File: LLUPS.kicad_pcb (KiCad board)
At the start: 2 copper layers, 90 x 58 mm, 39 parts, among them J1 USB_C, J2 Output, J3 Debug, Q1 FS8205A, U1 USBLC6-2SC6, U2 BQ24072, U3 HY2113-KB5B, U4 MT3608, U5 AP2112K-3.3, U6 LN61CN3302MR-G

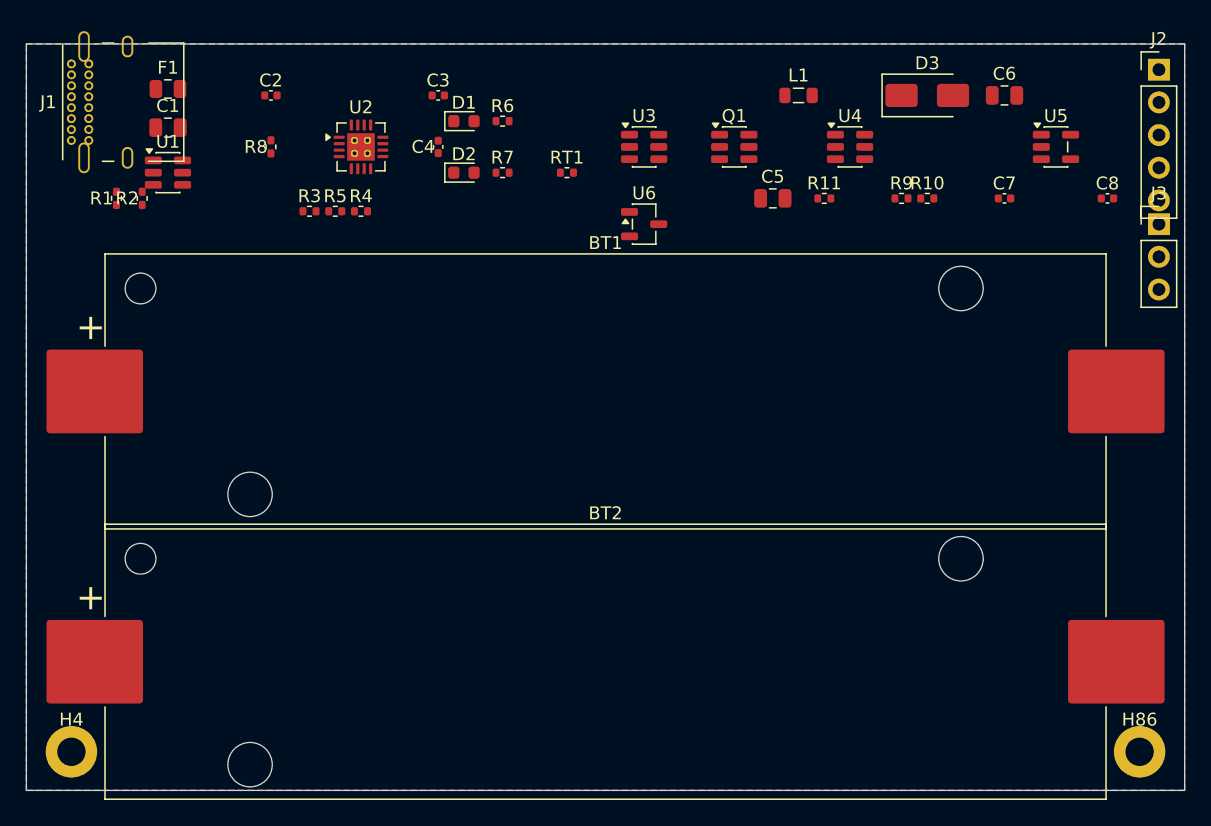
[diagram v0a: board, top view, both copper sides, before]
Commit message: Add PCB scoring framework and fix power trace widths
- scoring/ module with 6 checks: trace widths, DRC, connectivity,
  placement, vias, routing efficiency
- score_layout.py orchestrator with JSON output and --compare
- Fix power trace widths: 0.5mm → 1.0mm, 0.8mm → 1.2mm (spec: ≥1mm)
- Add 18 thermal vias under U2 (BQ24072) and U4 (MT3608)
- Score improved from 56.2 → 84.9/100

Co-Authored-By: Claude Opus 4.6 <noreply@anthropic.com>
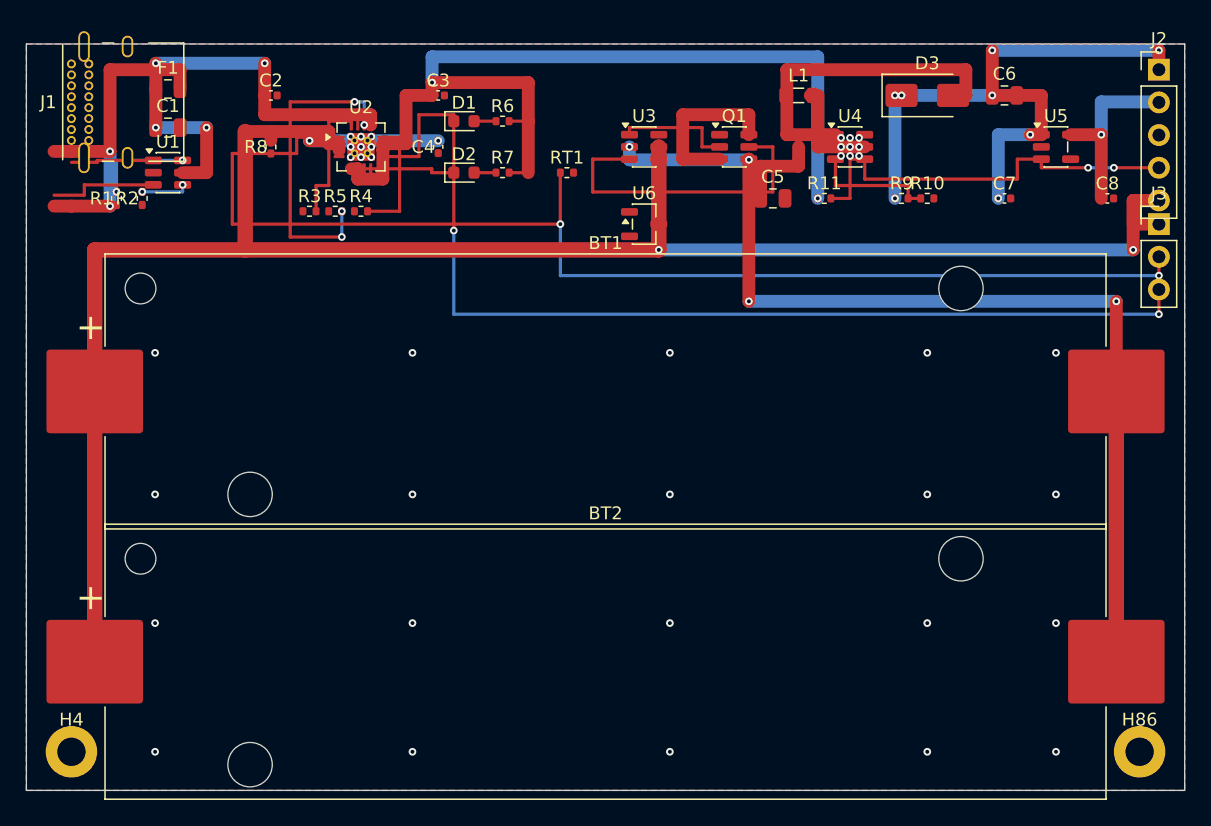
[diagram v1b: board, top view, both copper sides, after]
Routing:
- net /VBAT: track 0.00 -> 160.5 mm, vias 0 -> 4
- net /NTC_SENSE: track 0.00 -> 96.5 mm, vias 0 -> 2
- net /CHG_N: track 0.00 -> 81.0 mm, vias 0 -> 2
- net /CELL_NEG: track 0.00 -> 77.9 mm, vias 0 -> 4
- net /VSYS: track 0.00 -> 75.0 mm, vias 0 -> 2
- net /5V: track 0.00 -> 48.7 mm, vias 0 -> 8
- net /VBUS: track 0.00 -> 35.8 mm, vias 0 -> 4
- net /EN: track 0.00 -> 32.3 mm, vias 0 -> 2
- net Net-(F1-Pad2): track 0.00 -> 26.2 mm, vias 0 -> 2
- net Net-(D3-A): track 0.00 -> 25.7 mm
- net Net-(Q1B-G): track 0.00 -> 24.8 mm
- net Net-(U2-TMR): track 0.00 -> 24.1 mm, vias 0 -> 4
- net /VSYS_BOOST: track 0.00 -> 15.2 mm
- net /3V3: track 0.00 -> 14.4 mm, vias 0 -> 2
- net Net-(Q1A-D): track 0.00 -> 13.0 mm
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
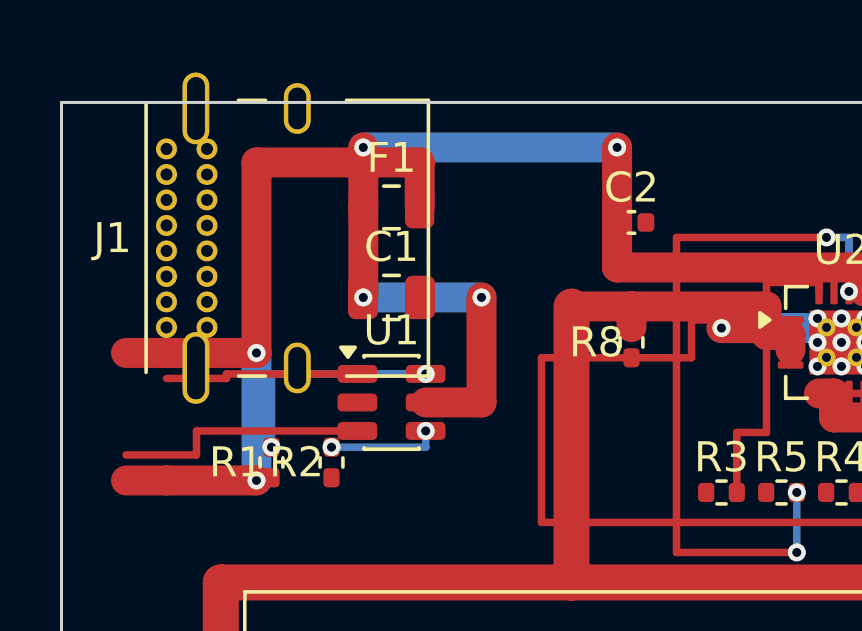
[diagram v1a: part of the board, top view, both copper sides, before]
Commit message: Wire up visual review pipeline and fix placement overlap detection
Add --review flag to score_layout.py that outputs render paths for Claude
to read and evaluate. Update SKILL.md with structured visual review
checklist. Fix placement_check to skip false-positive overlaps between
mechanical parts (batteries, mounting holes, connectors). Add
plot_scores.py for score history visualization.

Co-Authored-By: Claude Opus 4.6 <noreply@anthropic.com>
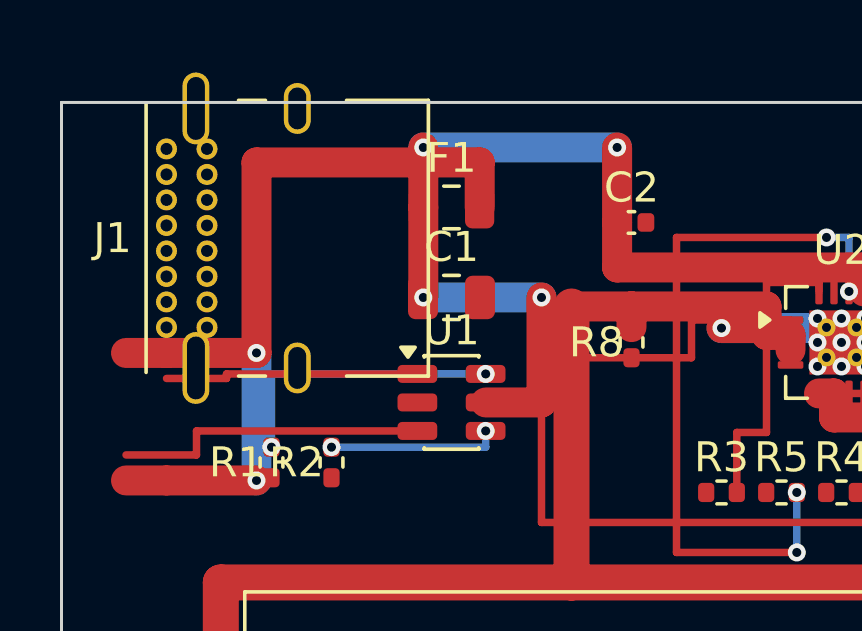
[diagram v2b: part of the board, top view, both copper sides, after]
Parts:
- moved C1 2.00 mm to (13.0, 6.50)
- moved F1 2.00 mm to (13.0, 3.50)
- moved U1 2.00 mm to (13.0, 10.0)
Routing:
- net Net-(R2-Pad1): track 3.68 -> 5.68 mm
- net Net-(R1-Pad1): track 7.58 -> 9.58 mm
- net Net-(J1-CC2): track 8.51 -> 10.5 mm
- net Net-(J1-CC1): track 6.51 -> 8.51 mm
- net Net-(F1-Pad2): track 26.2 -> 28.2 mm
- net /VBUS: track 35.8 -> 33.8 mm
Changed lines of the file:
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@@
 	(footprint "Fuse:Fuse_0805_2012Metric"
 		(layer "F.Cu")
-		(at 11 3.5)
+		(at 13 3.5)
 	(version 20241229)
 	(generator "kicad-footprint-generator")
@@
 	(footprint "Capacitor_SMD:C_0805_2012Metric"
 		(layer "F.Cu")
-		(at 11 6.5)
+		(at 13 6.5)
 	(version 20241229)
 	(generator "kicad-footprint-generator")
@@
 	(footprint "Package_TO_SOT_SMD:SOT-23-6"
 		(layer "F.Cu")
-		(at 11 10)
+		(at 13 10)
 	(version 20241229)
 	(generator "kicad-footprint-generator")
@@
 	(segment
 		(start 6.5 2)
-		(end 11.94 2)
+		(end 13.94 2)
 		(width 1.0)
 		(layer "F.Cu")
@@
 	)
 	(segment
-		(start 11.94 2)
-		(end 11.94 3.5)
+		(start 13.94 2)
+		(end 13.94 3.5)
 		(width 1.0)
 		(layer "F.Cu")
@@
 	)
 	(segment
-		(start 10.06 3.5)
-		(end 10.06 6.5)
+		(start 12.06 3.5)
+		(end 12.06 6.5)
 		(width 1.0)
 		(layer "F.Cu")
@@
 	)
 	(segment
-		(start 10.06 6.5)
-		(end 14 6.5)
+		(start 12.06 6.5)
+		(end 16 6.5)
 		(width 1.0)
 		(layer "B.Cu")
@@
 	)
 	(segment
-		(start 14 6.5)
-		(end 14 10)
+		(start 16 6.5)
+		(end 16 10)
 		(width 1.0)
 		(layer "F.Cu")
@@
 	)
 	(segment
-		(start 14 10)
-		(end 12.14 10)
+		(start 16 10)
+		(end 14.14 10)
 		(width 1.0)
 		(layer "F.Cu")
@@
 	)
 	(segment
-		(start 10.06 3.5)
-		(end 10.06 1.5)
+		(start 12.06 3.5)
+		(end 12.06 1.5)
 		(width 1.0)
 		(layer "F.Cu")
@@
 	)
 	(segment
-		(start 10.06 1.5)
+		(start 12.06 1.5)
 		(end 18.52 1.5)
 		(width 1.0)
@@
 	(segment
 		(start 5.5 9.05)
-		(end 9.86 9.05)
+		(end 11.86 9.05)
 		(width 0.25)
 		(layer "F.Cu")
@@
 	(segment
 		(start 4.5 10.95)
-		(end 9.86 10.95)
+		(end 11.86 10.95)
 		(width 0.25)
 		(layer "F.Cu")
@@
 	(segment
 		(start 7 9.05)
-		(end 12.14 9.05)
+		(end 14.14 9.05)
 		(width 0.25)
 		(layer "B.Cu")
@@
 	(segment
 		(start 9 11.49)
-		(end 12.14 11.49)
+		(end 14.14 11.49)
 		(width 0.25)
 		(layer "B.Cu")
@@
 	)
 	(segment
-		(start 12.14 11.49)
-		(end 12.14 10.95)
+		(start 14.14 11.49)
+		(end 14.14 10.95)
 		(width 0.25)
 		(layer "B.Cu")
@@
 	)
 	(via
-		(at 10.06 6.5)
+		(at 12.06 6.5)
 		(size 0.6)
 		(drill 0.3)
@@
 	)
 	(via
-		(at 14 6.5)
+		(at 16 6.5)
 		(size 0.6)
 		(drill 0.3)
@@
 	)
 	(via
-		(at 10.06 1.5)
+		(at 12.06 1.5)
 		(size 0.6)
 		(drill 0.3)
@@
 	)
 	(via
-		(at 12.14 9.05)
+		(at 14.14 9.05)
 		(size 0.6)
 		(drill 0.3)
@@
 	)
 	(via
-		(at 12.14 10.95)
+		(at 14.14 10.95)
 		(size 0.6)
 		(drill 0.3)

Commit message: Overhaul scoring with real DRC, add routing tools
Scoring changes:
- DRC check now runs kicad-cli for real violations instead of stored markers
- Logarithmic scoring so DRC improvements always register (no floor at 0)
- Rebalanced weights: DRC 0.35, placement 0.20, connectivity 0.15,
  traces 0.10, geometry 0.10, vias 0.10
- Always pass _pcb_path to config for DRC regardless of render flag

New routing tools:
- simple_router.py: clear-and-reroute with L-shape + via fallback
- cleanup_routing.py: remove dangling vias and crossing tracks
- reroute_net.py: surgically reroute individual nets to B.Cu
- add_gnd_zone.py: add GND copper pour on B.Cu

PCB: J1 USB-C moved to left board edge facing outward (270 deg)

Co-Authored-By: Claude Opus 4.6 <noreply@anthropic.com>
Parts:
- moved J1 2.50 mm to (1.00, 7.50), turned to -90 degrees

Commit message: Add compactness and footprint orientation scoring checks
New checks (advisory, weight=0 for now):
- CompactnessCheck: measures board fill ratio and grid occupancy,
  flags oversized boards with wasted space
- OrientationCheck: verifies connectors/switches/test points face
  outward from nearest board edge

PCB: rotate J2 (Output) and J3 (Debug) to face right edge outward.
All 3 connectors now pass orientation check.

Co-Authored-By: Claude Opus 4.6 <noreply@anthropic.com>
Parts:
- moved J2 1.00 mm to (89.0, 2.00), turned to 90 degrees
- moved J3 1.00 mm to (89.0, 14.0), turned to 90 degrees
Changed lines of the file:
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@@
 	(footprint "Connector_PinHeader_2.54mm:PinHeader_1x03_P2.54mm_Vertical"
 		(layer "F.Cu")
-		(at 88 14)
+		(at 89 14 90)
 		(descr "Through hole straight pin header, 1x03, 2.54mm pitch, single row")
 		(tags "Through hole pin header THT 1x03 2.54mm single row")
 		(property "Reference" "J3"
-			(at 0 -2.38 0)
+			(at 0 -2.38 90)
 			(layer "F.SilkS")
 			(effects
@@
 		)
 		(property "Value" "Debug"
-			(at 0 7.46 0)
+			(at 0 7.46 90)
 			(layer "F.Fab")
 			(effects
@@
 		)
 		(property "Datasheet" ""
-			(at 0 0 0)
+			(at 0 0 90)
 			(layer "F.Fab")
 			(hide yes)
@@
 		)
 		(property "Description" ""
-			(at 0 0 0)
+			(at 0 0 90)
 			(layer "F.Fab")
 			(hide yes)
@@
 		)
 		(fp_line
-			(start -1.38 1.27)
-			(end -1.38 6.46)
+			(start 1.38 1.27)
+			(end 1.38 6.46)
 			(stroke
 				(width 0.12)
@@
 		)
 		(fp_line
-			(start -1.38 6.46)
-			(end 1.38 6.46)
+			(start -1.38 1.27)
+			(end -1.38 6.46)
 			(stroke
 				(width 0.12)
@@
 		)
 		(fp_line
-			(start 1.38 1.27)
+			(start -1.38 6.46)
 			(end 1.38 6.46)
 			(stroke
@@
 		)
 		(fp_line
-			(start -1.27 -0.635)
-			(end -0.635 -1.27)
+			(start 1.27 -1.27)
+			(end 1.27 6.35)
 			(stroke
 				(width 0.1)
@@
 		)
 		(fp_line
-			(start -1.27 6.35)
-			(end -1.27 -0.635)
+			(start -0.635 -1.27)
+			(end 1.27 -1.27)
 			(stroke
 				(width 0.1)
@@
 		)
 		(fp_line
-			(start -0.635 -1.27)
-			(end 1.27 -1.27)
+			(start -1.27 -0.635)
+			(end -0.635 -1.27)
 			(stroke
 				(width 0.1)
@@
 		)
 		(fp_line
-			(start 1.27 -1.27)
-			(end 1.27 6.35)
+			(start 1.27 6.35)
+			(end -1.27 6.35)
 			(stroke
 				(width 0.1)
@@
 		)
 		(fp_line
-			(start 1.27 6.35)
-			(end -1.27 6.35)
+			(start -1.27 6.35)
+			(end -1.27 -0.635)
 			(stroke
 				(width 0.1)
@@
 		)
 		(fp_text user "${REFERENCE}"
-			(at 0 2.54 90)
+			(at 0 2.54 180)
 			(layer "F.Fab")
 			(effects
@@
 		)
 		(pad "1" thru_hole rect
-			(at 0 0)
+			(at 0 0 90)
 			(size 1.7 1.7)
 			(drill 1)
@@
 		)
 		(pad "2" thru_hole circle
-			(at 0 2.54)
+			(at 0 2.54 90)
 			(size 1.7 1.7)
 			(drill 1)
@@
 		)
 		(pad "3" thru_hole circle
-			(at 0 5.08)
+			(at 0 5.08 90)
 			(size 1.7 1.7)
 			(drill 1)
@@
 	(footprint "Connector_PinHeader_2.54mm:PinHeader_1x05_P2.54mm_Vertical"
 		(layer "F.Cu")
-		(at 88 2)
+		(at 89 2 90)
 		(descr "Through hole straight pin header, 1x05, 2.54mm pitch, single row")
 		(tags "Through hole pin header THT 1x05 2.54mm single row")
 		(property "Reference" "J2"
-			(at 0 -2.38 0)
+			(at 0 -2.38 90)
 			(layer "F.SilkS")
 			(effects
@@
 		)
 		(property "Value" "Output"
-			(at 0 12.54 0)
+			(at 0 12.54 90)
 			(layer "F.Fab")
 			(effects
@@
 		)
 		(property "Datasheet" ""
-			(at 0 0 0)
+			(at 0 0 90)
 			(layer "F.Fab")
 			(hide yes)
@@
 		)
 		(property "Description" ""
-			(at 0 0 0)
+			(at 0 0 90)
 			(layer "F.Fab")
 			(hide yes)
@@
 		)
 		(fp_line
-			(start -1.38 1.27)
-			(end -1.38 11.54)
+			(start 1.38 1.27)
+			(end 1.38 11.54)
 			(stroke
 				(width 0.12)
@@
 		)
 		(fp_line
-			(start -1.38 11.54)
-			(end 1.38 11.54)
+			(start -1.38 1.27)
+			(end -1.38 11.54)
 			(stroke
 				(width 0.12)
@@
 		)
 		(fp_line
-			(start 1.38 1.27)
+			(start -1.38 11.54)
 			(end 1.38 11.54)
 			(stroke
@@
 		)
 		(fp_line
-			(start -1.27 -0.635)
-			(end -0.635 -1.27)
+			(start 1.27 -1.27)
+			(end 1.27 11.43)
 			(stroke
 				(width 0.1)
@@
 		)
 		(fp_line
-			(start -1.27 11.43)
-			(end -1.27 -0.635)
+			(start -0.635 -1.27)
+			(end 1.27 -1.27)
 			(stroke
 				(width 0.1)
@@
 		)
 		(fp_line
-			(start -0.635 -1.27)
-			(end 1.27 -1.27)
+			(start -1.27 -0.635)
+			(end -0.635 -1.27)
 			(stroke
 				(width 0.1)
@@
 		)
 		(fp_line
-			(start 1.27 -1.27)
-			(end 1.27 11.43)
+			(start 1.27 11.43)
+			(end -1.27 11.43)
 			(stroke
 				(width 0.1)
@@
 		)
 		(fp_line
-			(start 1.27 11.43)
-			(end -1.27 11.43)
+			(start -1.27 11.43)
+			(end -1.27 -0.635)
 			(stroke
 				(width 0.1)
@@
 		)
 		(fp_text user "${REFERENCE}"
-			(at 0 5.08 90)
+			(at 0 5.08 180)
 			(layer "F.Fab")
 			(effects
@@
 		)
 		(pad "1" thru_hole rect
-			(at 0 0)
+			(at 0 0 90)
 			(size 1.7 1.7)
 			(drill 1)
@@
 		)
 		(pad "2" thru_hole circle
-			(at 0 2.54)
+			(at 0 2.54 90)
 			(size 1.7 1.7)
 			(drill 1)
@@
 		)
 		(pad "3" thru_hole circle
-			(at 0 5.08)
+			(at 0 5.08 90)
 			(size 1.7 1.7)
 			(drill 1)
@@
 		)
 		(pad "4" thru_hole circle
-			(at 0 7.62)
+			(at 0 7.62 90)
 			(size 1.7 1.7)
 			(drill 1)
@@
 		)
 		(pad "5" thru_hole circle
-			(at 0 10.16)
+			(at 0 10.16 90)
 			(size 1.7 1.7)
 			(drill 1)

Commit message: 25-round experiment: best score 2.52, dashboard updated, GIF dropped (no-render run)
Co-Authored-By: Claude Sonnet 4.6 <noreply@anthropic.com>
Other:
- board size 90 x 58 mm -> 140 x 90 mm
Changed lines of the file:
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@@
 	(gr_rect
 		(start 0 0)
-		(end 90 58)
+		(end 140 90)
 		(stroke
 			(width 0.1)
